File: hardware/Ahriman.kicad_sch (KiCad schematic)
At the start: 111 parts, among them J1 Power_In, J10 USB3145-30-1-A, J2 SWD_Debug, J3 UART_Debug, J4 POT1, J5 PB_Foot, J6 POT2, J7 POT3, J8 Analog_In, J9 Analog_Out, Q1 T2N7002AK, Q2 T2N7002AK, Q3 T2N7002AK, SW1 PTS636, U1 EFM32TG11B520F128GM64-A, U2 NE5532, U3 UA78M33CKVURG3, U4 GD25Q80CSIGR, U5 NAU88C10YG, U6 AD8034ARZ, U7 74AHC1G14, U8 SP0503BAHTG, U9 CP2110-F01-GM, Y1 12.0MHz

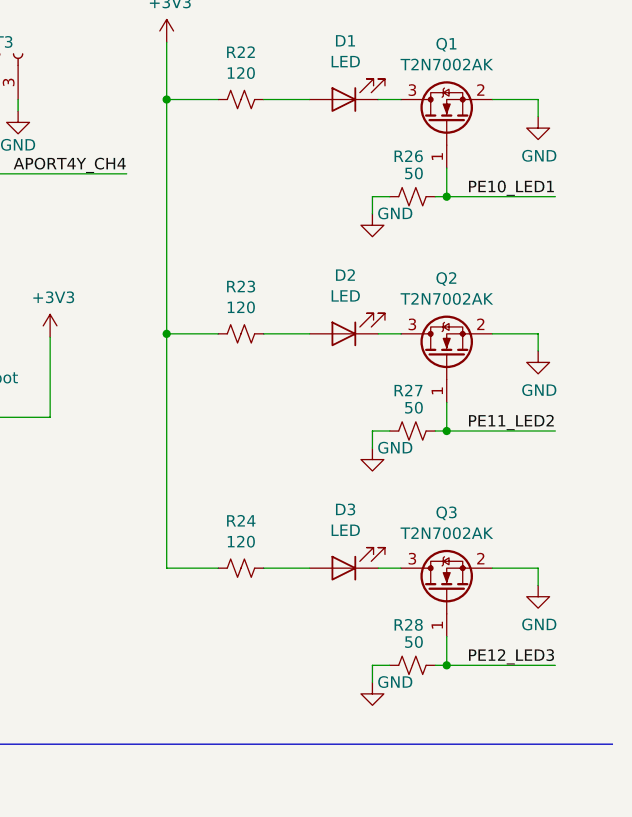
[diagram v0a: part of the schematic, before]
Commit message: Re-organize File Structure
Start ignoring unwanted files
Create BOM
Re-organize files
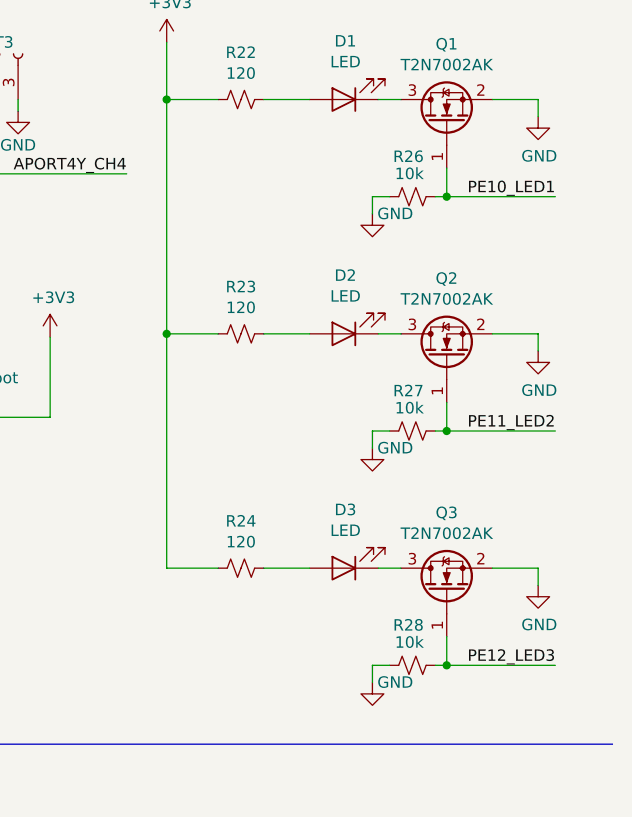
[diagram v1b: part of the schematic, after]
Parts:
- R26, R27, R28: value 50 -> 10k
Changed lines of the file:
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@@
       (effects (font (size 1.27 1.27)) (justify left))
     )
-    (property "Value" "50" (id 1) (at 398.78 69.215 90)
+    (property "Value" "10k" (id 1) (at 398.78 69.215 90)
       (effects (font (size 1.27 1.27)) (justify left))
     )
@@
       (effects (font (size 1.27 1.27)) (justify left))
     )
-    (property "Value" "50" (id 1) (at 398.78 95.25 90)
+    (property "Value" "10k" (id 1) (at 398.78 95.25 90)
       (effects (font (size 1.27 1.27)) (justify left))
     )
@@
       (effects (font (size 1.27 1.27)) (justify left))
     )
-    (property "Value" "50" (id 1) (at 398.78 43.18 90)
+    (property "Value" "10k" (id 1) (at 398.78 43.18 90)
       (effects (font (size 1.27 1.27)) (justify left))
     )
@@
     )
     (path "/00000000-0000-0000-0000-00006390df66"
-      (reference "R26") (unit 1) (value "50") (footprint "Resistor_SMD:R_0603_1608Metric")
+      (reference "R26") (unit 1) (value "10k") (footprint "Resistor_SMD:R_0603_1608Metric")
     )
     (path "/00000000-0000-0000-0000-000063799436"
-      (reference "R27") (unit 1) (value "50") (footprint "Resistor_SMD:R_0603_1608Metric")
+      (reference "R27") (unit 1) (value "10k") (footprint "Resistor_SMD:R_0603_1608Metric")
     )
     (path "/00000000-0000-0000-0000-0000638e5724"
-      (reference "R28") (unit 1) (value "50") (footprint "Resistor_SMD:R_0603_1608Metric")
+      (reference "R28") (unit 1) (value "10k") (footprint "Resistor_SMD:R_0603_1608Metric")
     )
     (path "/6013f858-c48b-4bf4-8b16-64b50c0c29db"
